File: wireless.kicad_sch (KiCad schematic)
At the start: 37 parts, among them J1301 u.FL, U1301 LBEE5KL1YN-814

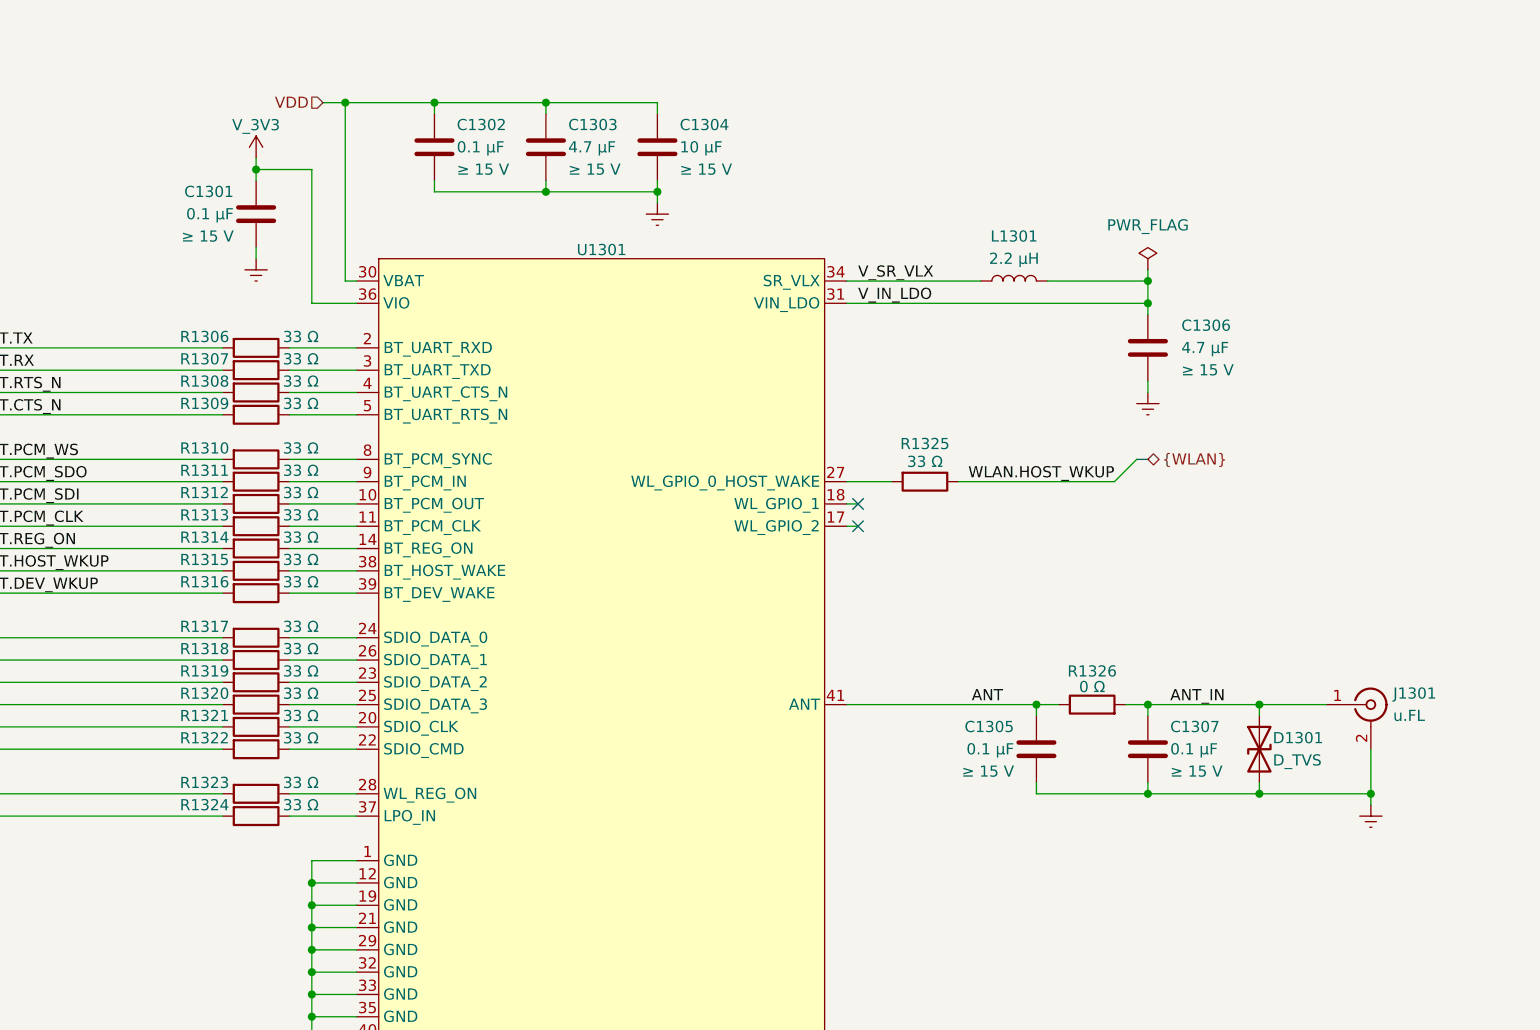
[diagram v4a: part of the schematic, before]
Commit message: Fix component values
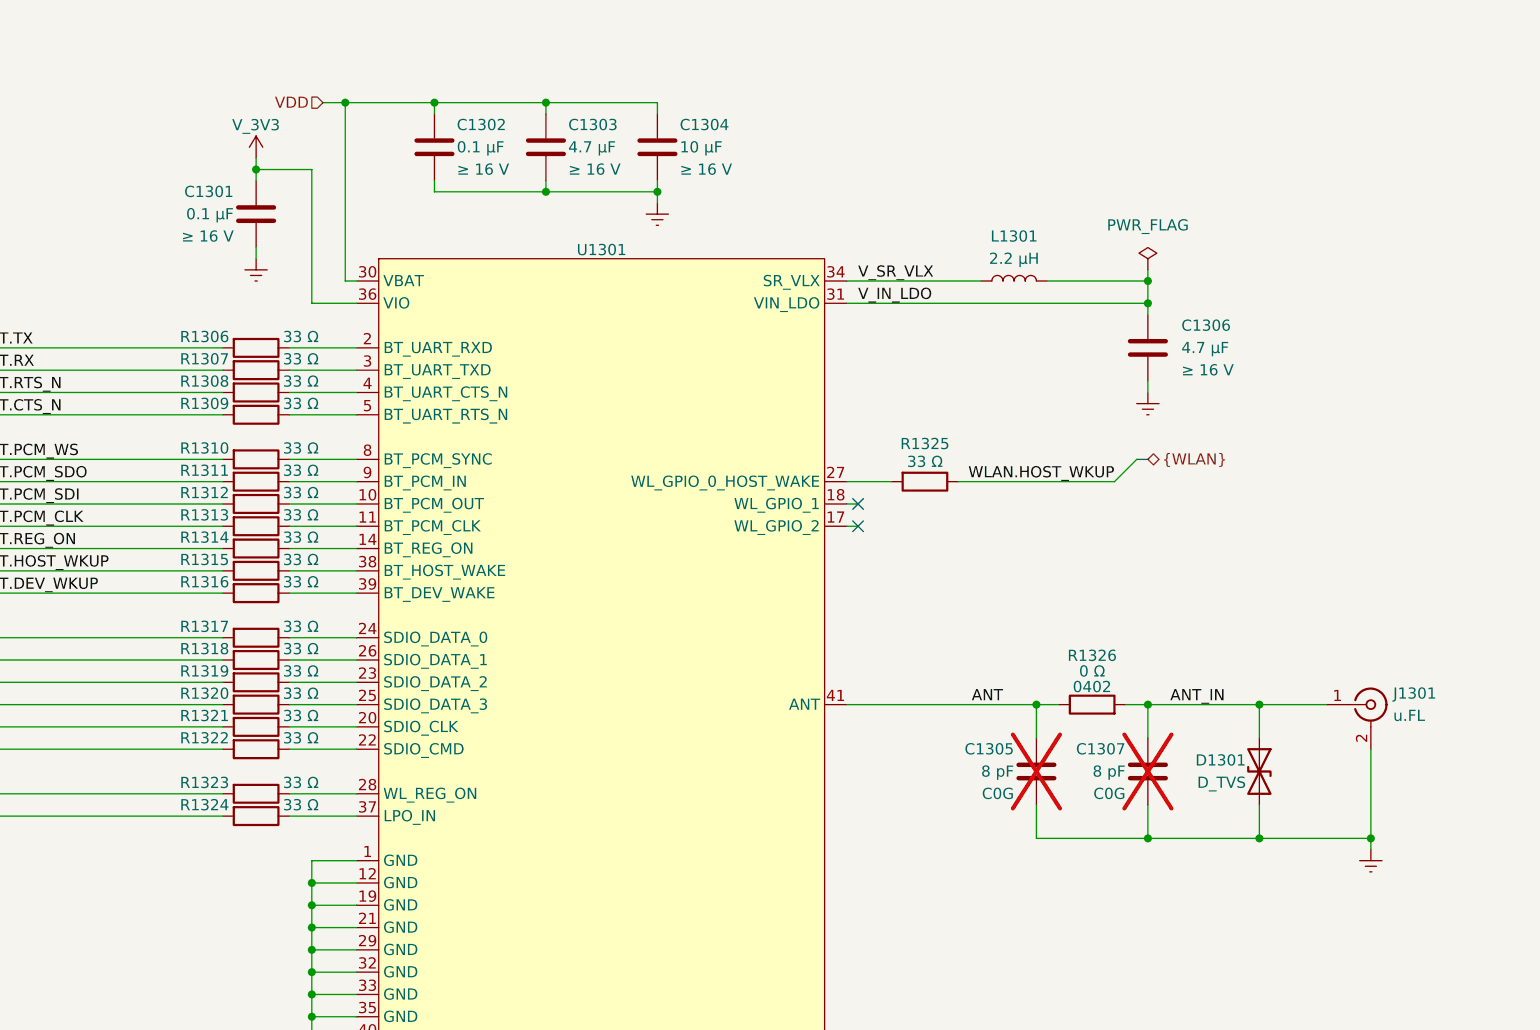
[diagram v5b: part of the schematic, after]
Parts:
- C1301, C1302, C1303, C1304, C1306: Voltage rating ≥ 15 V -> ≥ 16 V
- C1305, C1307: value 0.1 µF -> 8 pF; Temperature coefficient (none) -> C0G; Voltage rating ≥ 15 V -> (none); now not fitted
- R1326: Size (none) -> 0402
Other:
- moved on the sheet: D1301

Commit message: Clean-up schematics
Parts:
- R1306, R1307, R1308, R1309, R1310, R1311, R1312, R1313, R1314, R1315, R1316, R1317, R1318, R1319, R1320, R1321, R1322, R1323, R1324, R1325: value 33 Ω -> 0 Ω
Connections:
- net VDD: now also C1301.1, U1301.36 (VIO); no longer C1302.1, C1303.1, C1304.1, U1301.30 (VBAT)
- net V_3V3: now also C1302.1, C1303.1, C1304.1, U1301.30 (VBAT); no longer C1301.1, U1301.36 (VIO)
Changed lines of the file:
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@@
 		)
 	)
+	(wire
+		(pts
+			(xy 175.26 114.3) (xy 177.8 114.3)
+		)
+		(stroke
+			(width 0)
+			(type default)
+		)
+	)
 	(bus
 		(pts
@@
 	(wire
 		(pts
-			(xy 101.6 175.26) (xy 173.99 175.26)
+			(xy 187.96 105.41) (xy 187.96 106.68)
 		)
 		(stroke
@@
 	(wire
 		(pts
-			(xy 181.61 162.56) (xy 189.23 162.56)
+			(xy 101.6 175.26) (xy 173.99 175.26)
 		)
 		(stroke
@@
 	(wire
 		(pts
-			(xy 245.11 220.98) (xy 246.38 220.98)
+			(xy 181.61 162.56) (xy 189.23 162.56)
 		)
 		(stroke
@@
 	(wire
 		(pts
-			(xy 139.7 167.64) (xy 173.99 167.64)
+			(xy 245.11 220.98) (xy 246.38 220.98)
 		)
 		(stroke
@@
 	(wire
 		(pts
-			(xy 74.93 175.26) (xy 101.6 175.26)
+			(xy 139.7 167.64) (xy 173.99 167.64)
 		)
 		(stroke
@@
 	(wire
 		(pts
-			(xy 184.15 210.82) (xy 184.15 213.36)
+			(xy 74.93 175.26) (xy 101.6 175.26)
 		)
 		(stroke
@@
 	(wire
 		(pts
-			(xy 101.6 153.67) (xy 114.3 153.67)
+			(xy 184.15 210.82) (xy 184.15 213.36)
 		)
 		(stroke
@@
 	(wire
 		(pts
-			(xy 245.11 175.26) (xy 266.7 175.26)
+			(xy 101.6 153.67) (xy 114.3 153.67)
 		)
 		(stroke
@@
 	(wire
 		(pts
-			(xy 177.8 113.03) (xy 177.8 114.3)
+			(xy 245.11 175.26) (xy 266.7 175.26)
 		)
 		(stroke
@@
 	(wire
 		(pts
-			(xy 185.42 106.68) (xy 187.96 106.68)
-		)
-		(stroke
-			(width 0)
-			(type default)
-		)
-	)
-	(wire
-		(pts
 			(xy 181.61 170.18) (xy 189.23 170.18)
 		)
@@
 	(hierarchical_label "VDD"
 		(shape input)
-		(at 185.42 106.68 180)
+		(at 175.26 114.3 180)
 		(effects
 			(font
@@
 		(polyline
 			(pts
+				(xy 151.13 166.37) (xy 153.67 166.37) (xy 153.67 181.61) (xy 151.13 181.61)
+			)
+			(stroke
+				(width 0)
+				(type dash)
+			)
+			(fill
+				(type none)
+			)
+		)
+	)
+	(rule_area
+		(polyline
+			(pts
 				(xy 291.465 166.37) (xy 291.465 177.8) (xy 254.635 177.8) (xy 254.635 166.37)
 			)
@@
 		(length 2.54)
 		(shape round)
+		(at 152.4 181.61 180)
+		(fields_autoplaced yes)
+		(effects
+			(font
+				(size 1.27 1.27)
+			)
+			(justify right bottom)
+		)
+		(property "Netclass" "WLAN"
+			(at 153.0985 184.15 0)
+			(effects
+				(font
+					(size 1.27 1.27)
+				)
+				(justify left)
+			)
+		)
+		(property "Component Class" ""
+			(at -77.47 35.56 0)
+			(effects
+				(font
+					(size 1.27 1.27)
+					(italic yes)
+				)
+			)
+		)
+	)
+	(netclass_flag ""
+		(length 2.54)
+		(shape round)
 		(at 273.05 166.37 0)
 		(fields_autoplaced yes)
@@
 			)
 		)
-		(property "Value" "33 Ω"
+		(property "Value" "0 Ω"
 			(at 180.848 167.132 90)
 			(effects
@@
 			)
 		)
-		(property "Value" "33 Ω"
+		(property "Value" "0 Ω"
 			(at 180.848 139.192 90)
 			(effects
@@
 			)
 		)
-		(property "Value" "33 Ω"
+		(property "Value" "0 Ω"
 			(at 180.848 162.052 90)
 			(effects
@@
 			)
 		)
-		(property "Value" "33 Ω"
+		(property "Value" "0 Ω"
 			(at 180.848 184.912 90)
 			(effects
@@
 		(dnp no)
 		(fields_autoplaced yes)
-		(property "Reference" "#PWR01302"
+		(property "Reference" "#PWR01301"
 			(at 177.8 130.81 0)
 			(effects
@@
 			(project "linux-sbc"
 				(path "/fa11a02f-8043-4153-ab69-88d766503017/24c9b83b-271d-4c51-b843-406c618d8ce8"
-					(reference "#PWR01302")
+					(reference "#PWR01301")
 					(unit 1)
 				)
@@
 			)
 		)
-		(property "Value" "33 Ω"
+		(property "Value" "0 Ω"
 			(at 180.848 141.732 90)
 			(effects
@@
 			)
 		)
-		(property "Value" "33 Ω"
+		(property "Value" "0 Ω"
 			(at 180.848 174.752 90)
 			(effects
@@
 			)
 		)
-		(property "Value" "33 Ω"
+		(property "Value" "0 Ω"
 			(at 180.848 172.212 90)
 			(effects
@@
 			)
 		)
-		(property "Value" "33 Ω"
+		(property "Value" "0 Ω"
 			(at 180.848 159.512 90)
 			(effects
@@
 			)
 		)
-		(property "Value" "33 Ω"
+		(property "Value" "0 Ω"
 			(at 180.848 187.452 90)
 			(effects
@@
 			)
 		)
-		(property "Value" "33 Ω"
+		(property "Value" "0 Ω"
 			(at 180.848 169.672 90)
 			(effects
@@
 			)
 		)
-		(property "Value" "33 Ω"
+		(property "Value" "0 Ω"
 			(at 254 148.336 90)
 			(effects
@@
 			)
 		)
-		(property "Value" "33 Ω"
+		(property "Value" "0 Ω"
 			(at 180.848 177.292 90)
 			(effects
@@
 			)
 		)
-		(property "Value" "33 Ω"
+		(property "Value" "0 Ω"
 			(at 180.848 151.892 90)
 			(effects
@@
 	(symbol
 		(lib_id "power:VCC")
-		(at 177.8 113.03 0)
+		(at 187.96 105.41 0)
 		(unit 1)
 		(exclude_from_sim no)
@@
 		(on_board yes)
 		(dnp no)
-		(property "Reference" "#PWR01301"
-			(at 177.8 116.84 0)
+		(property "Reference" "#PWR01303"
+			(at 187.96 109.22 0)
 			(effects
 				(font
@@
 		)
 		(property "Value" "V_3V3"
-			(at 177.8 109.982 0)
+			(at 187.96 102.362 0)
 			(effects
 				(font
@@
 		)
 		(property "Footprint" ""
-			(at 177.8 113.03 0)
+			(at 187.96 105.41 0)
 			(effects
 				(font
@@
 		)
 		(property "Datasheet" ""
-			(at 177.8 113.03 0)
+			(at 187.96 105.41 0)
 			(effects
 				(font
@@
 		)
 		(property "Description" "Power symbol creates a global label with name \"VCC\""
-			(at 177.8 113.03 0)
+			(at 187.96 105.41 0)
 			(effects
 				(font
@@
 			(project "linux-sbc"
 				(path "/fa11a02f-8043-4153-ab69-88d766503017/24c9b83b-271d-4c51-b843-406c618d8ce8"
-					(reference "#PWR01301")
+					(reference "#PWR01303")
 					(unit 1)
 				)
@@
 			)
 		)
-		(property "Value" "33 Ω"
+		(property "Value" "0 Ω"
 			(at 180.848 154.432 90)
 			(effects
@@
 			)
 		)
-		(property "Value" "33 Ω"
+		(property "Value" "0 Ω"
 			(at 180.848 179.832 90)
 			(effects
@@
 			)
 		)
-		(property "Value" "33 Ω"
+		(property "Value" "0 Ω"
 			(at 180.848 149.352 90)
 			(effects
@@
 		(dnp no)
 		(fields_autoplaced yes)
-		(property "Reference" "#PWR01303"
+		(property "Reference" "#PWR01302"
 			(at 184.15 233.68 0)
 			(effects
@@
 			(project "linux-sbc"
 				(path "/fa11a02f-8043-4153-ab69-88d766503017/24c9b83b-271d-4c51-b843-406c618d8ce8"
-					(reference "#PWR01303")
+					(reference "#PWR01302")
 					(unit 1)
 				)
@@
 			)
 		)
-		(property "Value" "33 Ω"
+		(property "Value" "0 Ω"
 			(at 180.848 156.972 90)
 			(effects
@@
 			)
 		)
-		(property "Value" "33 Ω"
+		(property "Value" "0 Ω"
 			(at 180.848 134.112 90)
 			(effects
@@
 			)
 		)
-		(property "Value" "33 Ω"
+		(property "Value" "0 Ω"
 			(at 180.848 136.652 90)
 			(effects
@@
 			)
 		)
-		(property "Value" "33 Ω"
+		(property "Value" "0 Ω"
 			(at 180.848 146.812 90)
 			(effects

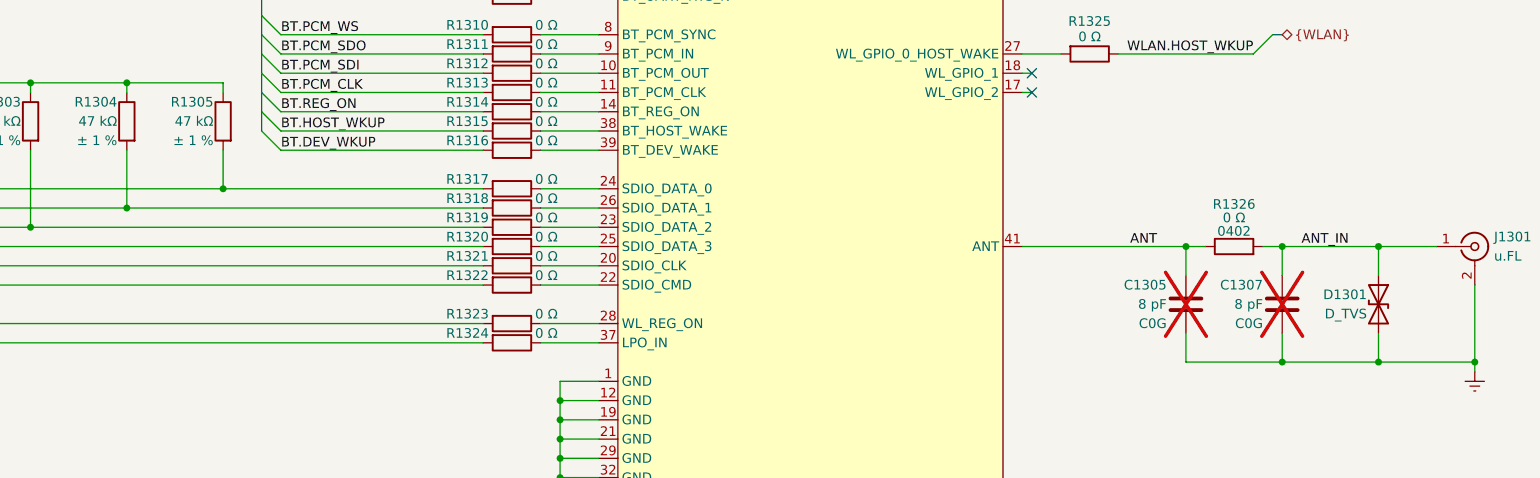
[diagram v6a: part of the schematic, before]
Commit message: Redo MPU pinout using STM32CubeMx
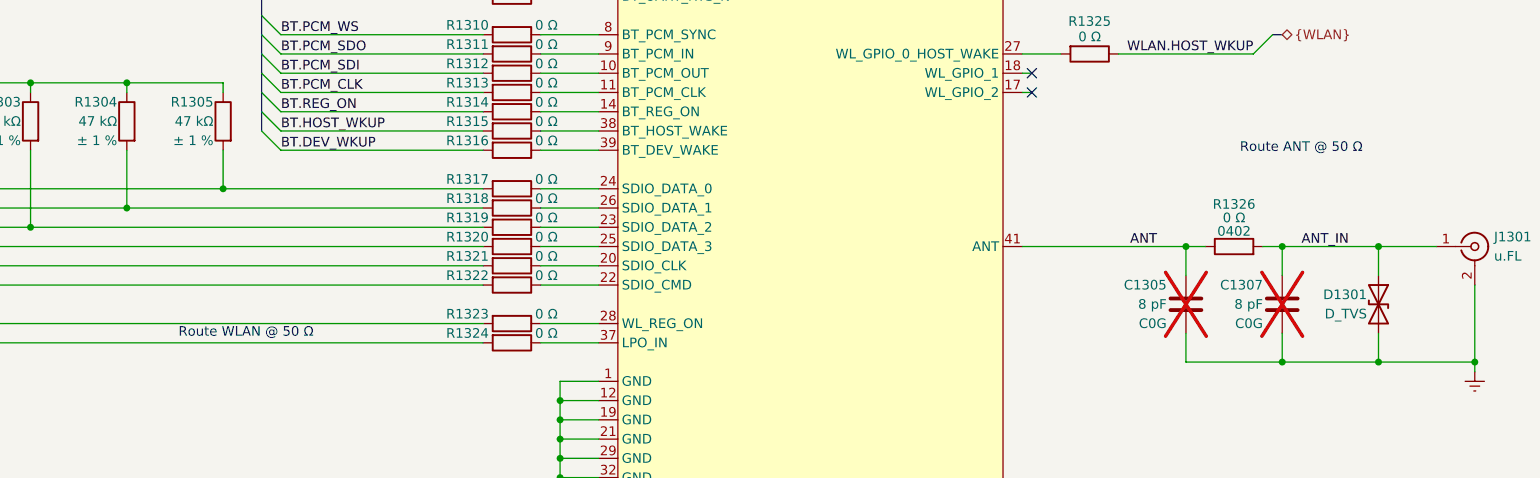
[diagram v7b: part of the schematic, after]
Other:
- note added: "Route ANT @ 50 Ω"
- note added: "Route WLAN @ 50 Ω"
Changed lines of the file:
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@@
 		(members "WLAN.D[0..3]" "WLAN.CMD" "WLAN.CLK" "WLAN.REG_ON" "WLAN.HOST_WKUP")
+	)
+	(text "Route ANT @ 50 Ω"
+		(exclude_from_sim no)
+		(at 273.812 162.306 0)
+		(effects
+			(font
+				(size 1.27 1.27)
+				(color 194 0 194 1)
+			)
+			(justify left)
+		)
+	)
+	(text "Route WLAN @ 50 Ω"
+		(exclude_from_sim no)
+		(at 151.638 186.69 0)
+		(effects
+			(font
+				(size 1.27 1.27)
+				(color 194 0 194 1)
+			)
+			(justify right)
+		)
 	)
 	(text_box "Notes"
@@
 		)
 		(property "Netclass" "WLAN"
-			(at 153.0985 184.15 0)
+			(at 151.7015 184.15 0)
 			(effects
 				(font
 					(size 1.27 1.27)
 				)
-				(justify left)
+				(justify right)
 			)
 		)
 		(property "Component Class" ""
-			(at -77.47 35.56 0)
+			(at 382.27 35.56 0)
 			(effects
 				(font
@@
 					(italic yes)
 				)
-			)
-		)
+				(justify left)
+			)
+		)

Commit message: Wireless: Set SR_VLX inductor BOM info
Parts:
- L1301: footprint (none) -> Inductor_SMD:L_0603_1608Metric; Digi-Key Part Number (none) -> 490-14478-1-ND; MPN (none) -> LQM18PN2R2MGHD; Manufacturer (none) -> Murata Electronics
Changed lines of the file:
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@@
 			)
 		)
-		(property "Footprint" ""
+		(property "Footprint" "Inductor_SMD:L_0603_1608Metric"
 			(at 264.16 127 0)
 			(effects
@@
 			)
 		)
-		(property "Datasheet" "~"
+		(property "Datasheet" "https://search.murata.co.jp/Ceramy/image/img/P02/JELF243B-0047.pdf"
 			(at 264.16 127 0)
 			(effects
@@
 			)
 		)
-		(property "Description" "Inductor"
+		(property "Description" "2.2 µH Shielded Multilayer Inductor 1.05 A 250mOhm Max 0603 (1608 Metric)"
 			(at 264.16 127 0)
 			(effects
 				(font
+					(size 1.27 1.27)
+				)
+				(hide yes)
+			)
+		)
+		(property "Digi-Key Part Number" "490-14478-1-ND"
+			(at 264.16 127 90)
+			(effects
+				(font
+					(size 1.27 1.27)
+				)
+				(hide yes)
+			)
+		)
+		(property "Manufacturer" "Murata Electronics"
+			(at 264.16 127 90)
+			(effects
+				(font
+					(size 1.27 1.27)
+				)
+				(hide yes)
+			)
+		)
+		(property "MPN" "LQM18PN2R2MGHD"
+			(at 264.16 127 90)
+			(effects
+				(font
